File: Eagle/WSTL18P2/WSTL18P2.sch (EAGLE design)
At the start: 22 parts, among them CON1 1X6CONN-1.27-ROUND, CON2 1X6CONN-1.27-ROUND, CON3 1X6CONN-1.27-ROUND, CON4 1X6CONN-1.27-ROUND, T1 ABS07AIG

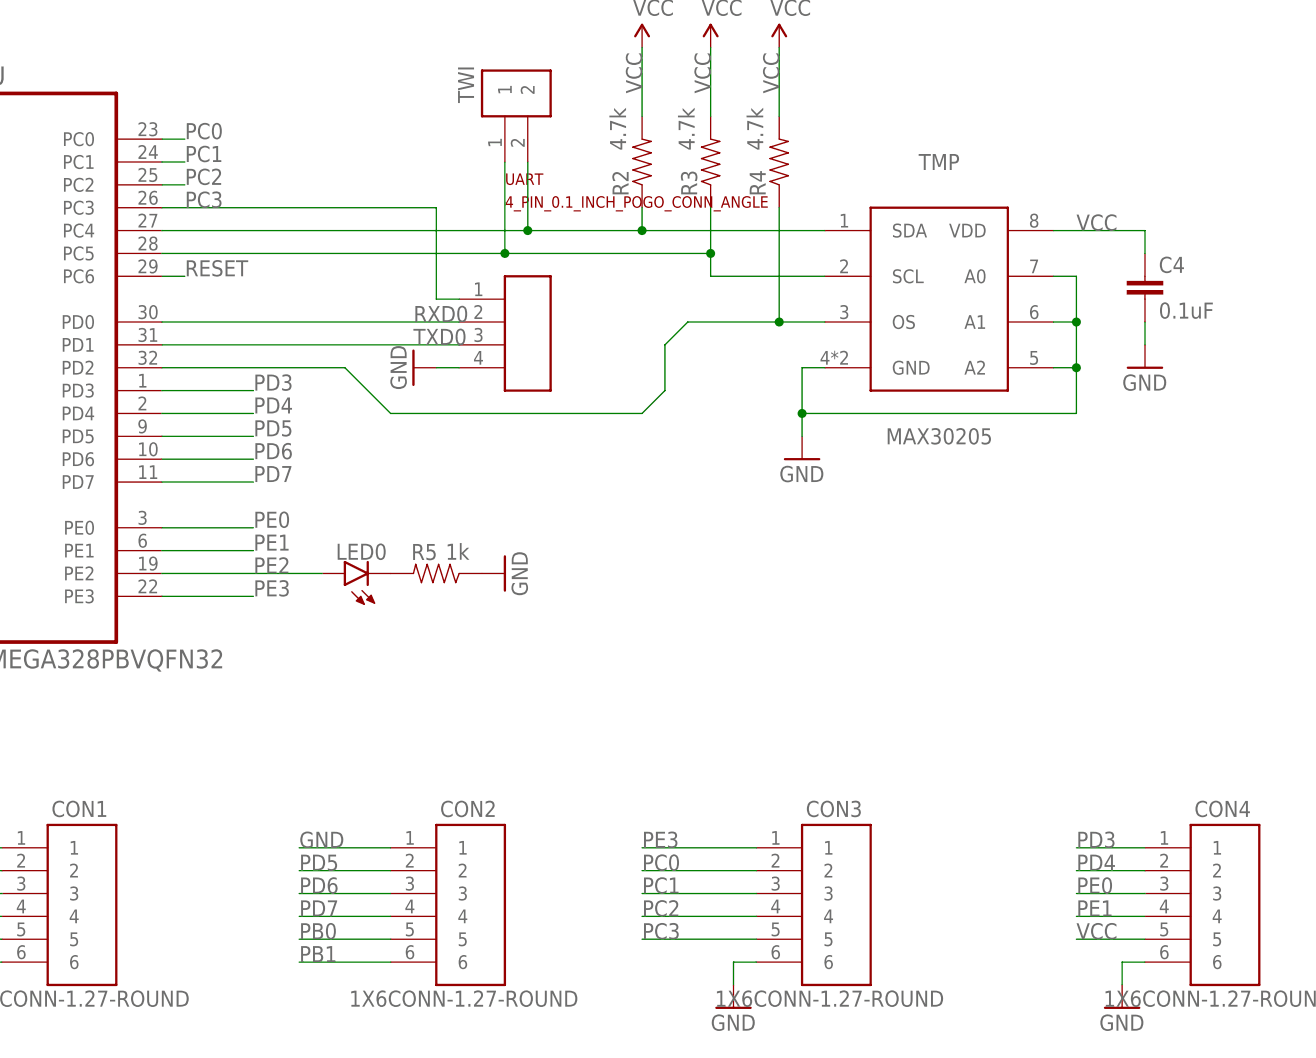
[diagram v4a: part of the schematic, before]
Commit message: Making TWI (I2C) pins available on perimeter headers
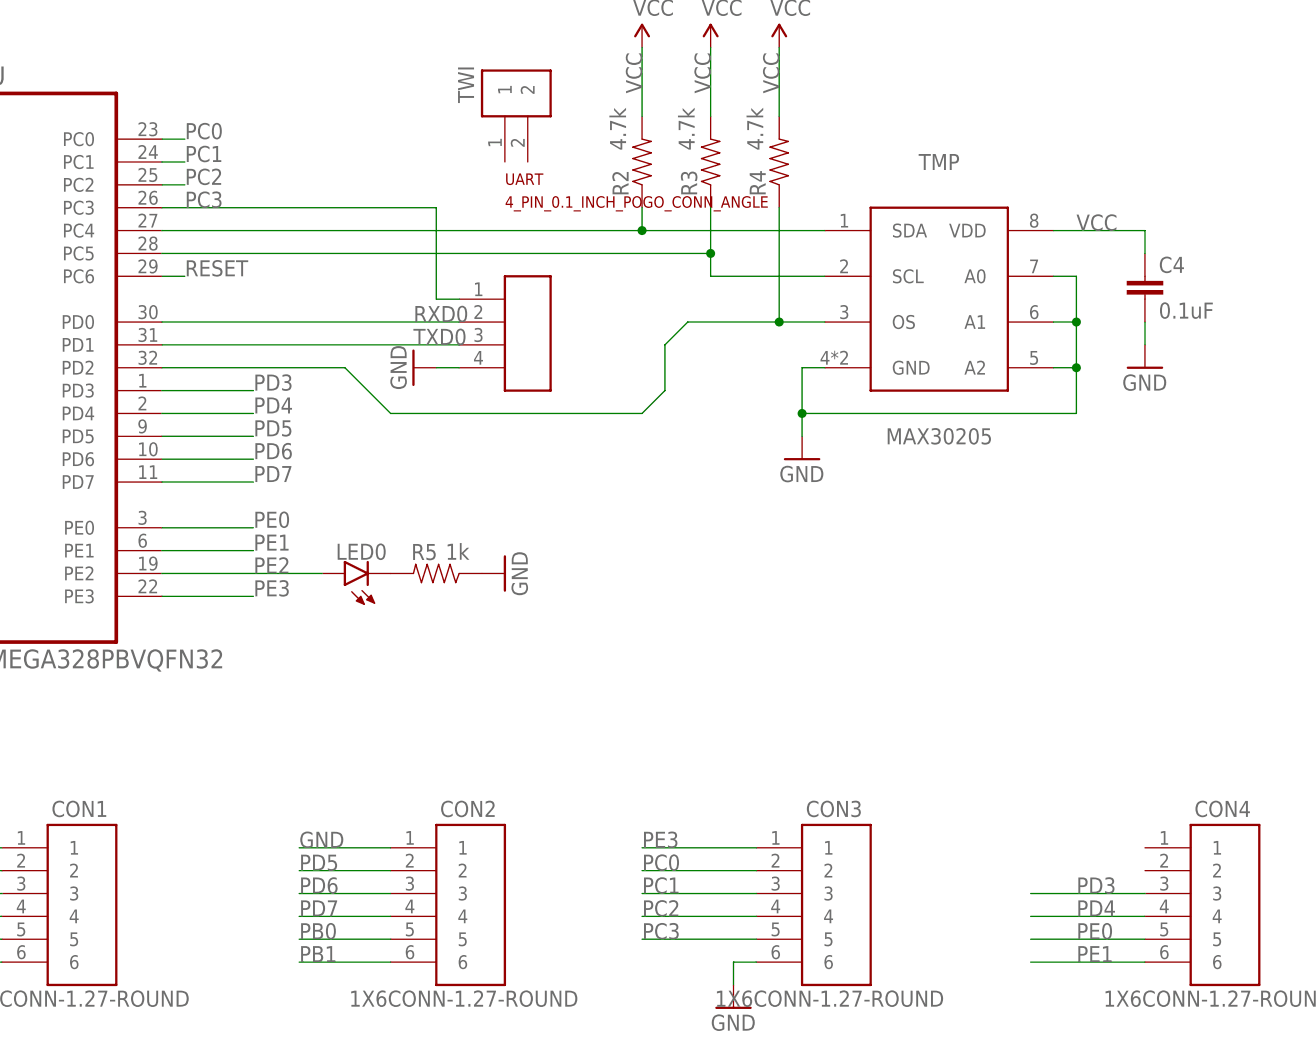
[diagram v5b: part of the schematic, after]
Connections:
- net GND: no longer CON4.6
- net PD3: now also CON4.3; no longer CON4.1
- net PD4: now also CON4.4; no longer CON4.2
- net PE0: now also CON4.5; no longer CON4.3
- net PE1: now also CON4.6; no longer CON4.4
- net SCL0: no longer TWI.1
- net SDA0: no longer TWI.2
- net VCC: no longer CON4.5
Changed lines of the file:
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@@
 <part name="GND9" library="SparkFun-Aesthetics" deviceset="GND" device=""/>
 <part name="CON4" library="AVR_ISP_127" deviceset="1X6CONN-1.27-ROUND" device=""/>
-<part name="GND10" library="SparkFun-Aesthetics" deviceset="GND" device=""/>
 <part name="VCC" library="SparkFun-Aesthetics" deviceset="5V" device="" value="VCC"/>
 <part name="GND11" library="SparkFun-Aesthetics" deviceset="GND" device=""/>
@@
 <instance part="GND9" gate="1" x="149.86" y="-25.4"/>
 <instance part="CON4" gate="G$1" x="205.74" y="-10.16"/>
-<instance part="GND10" gate="1" x="193.04" y="-25.4"/>
 <instance part="VCC" gate="G$1" x="-76.2" y="76.2"/>
 <instance part="GND11" gate="1" x="114.3" y="45.72" rot="R270"/>
@@
 <wire x1="139.7" y1="63.5" x2="139.7" y2="60.96" width="0.1524" layer="91"/>
 <pinref part="MCU" gate="A" pin="PC4"/>
-<wire x1="86.36" y1="60.96" x2="127" y2="60.96" width="0.1524" layer="91"/>
+<wire x1="86.36" y1="60.96" x2="139.7" y2="60.96" width="0.1524" layer="91"/>
 <pinref part="TMP" gate="G$1" pin="SDA"/>
-<wire x1="127" y1="60.96" x2="139.7" y2="60.96" width="0.1524" layer="91"/>
 <wire x1="139.7" y1="60.96" x2="160.02" y2="60.96" width="0.1524" layer="91"/>
 <junction x="139.7" y="60.96"/>
-<pinref part="TWI" gate="G$1" pin="2"/>
-<wire x1="127" y1="68.58" x2="127" y2="60.96" width="0.1524" layer="91"/>
-<junction x="127" y="60.96"/>
 </segment>
 </net>
@@
 <pinref part="R3" gate="G$1" pin="2"/>
 <pinref part="MCU" gate="A" pin="PC5"/>
-<wire x1="86.36" y1="58.42" x2="124.46" y2="58.42" width="0.1524" layer="91"/>
+<wire x1="86.36" y1="58.42" x2="147.32" y2="58.42" width="0.1524" layer="91"/>
 <pinref part="TMP" gate="G$1" pin="SCL"/>
-<wire x1="124.46" y1="58.42" x2="147.32" y2="58.42" width="0.1524" layer="91"/>
 <wire x1="160.02" y1="55.88" x2="147.32" y2="55.88" width="0.1524" layer="91"/>
 <wire x1="147.32" y1="58.42" x2="147.32" y2="55.88" width="0.1524" layer="91"/>
 <wire x1="147.32" y1="63.5" x2="147.32" y2="58.42" width="0.1524" layer="91"/>
 <junction x="147.32" y="58.42"/>
-<pinref part="TWI" gate="G$1" pin="1"/>
-<wire x1="124.46" y1="68.58" x2="124.46" y2="58.42" width="0.1524" layer="91"/>
-<junction x="124.46" y="58.42"/>
 </segment>
 </net>
@@
 <wire x1="68.58" y1="-7.62" x2="60.96" y2="-7.62" width="0.1524" layer="91"/>
 <label x="60.96" y="-7.62" size="1.778" layer="95"/>
-</segment>
-<segment>
-<pinref part="CON4" gate="G$1" pin="5"/>
-<wire x1="195.58" y1="-17.78" x2="187.96" y2="-17.78" width="0.1524" layer="91"/>
-<label x="187.96" y="-17.78" size="1.778" layer="95"/>
 </segment>
 <segment>
@@
 </segment>
 <segment>
-<pinref part="CON4" gate="G$1" pin="6"/>
-<wire x1="195.58" y1="-20.32" x2="193.04" y2="-20.32" width="0.1524" layer="91"/>
-<pinref part="GND10" gate="1" pin="GND"/>
-<wire x1="193.04" y1="-22.86" x2="193.04" y2="-20.32" width="0.1524" layer="91"/>
-</segment>
-<segment>
 <pinref part="GND11" gate="1" pin="GND"/>
 <pinref part="UART" gate="G$1" pin="4"/>
@@
 </segment>
 <segment>
-<pinref part="CON4" gate="G$1" pin="1"/>
-<wire x1="195.58" y1="-7.62" x2="187.96" y2="-7.62" width="0.1524" layer="91"/>
-<label x="187.96" y="-7.62" size="1.778" layer="95"/>
+<label x="187.96" y="-12.7" size="1.778" layer="95"/>
+<wire x1="182.88" y1="-12.7" x2="195.58" y2="-12.7" width="0.1524" layer="91"/>
+<pinref part="CON4" gate="G$1" pin="3"/>
 </segment>
 </net>
@@
 </segment>
 <segment>
-<pinref part="CON4" gate="G$1" pin="2"/>
-<wire x1="195.58" y1="-10.16" x2="187.96" y2="-10.16" width="0.1524" layer="91"/>
-<label x="187.96" y="-10.16" size="1.778" layer="95"/>
+<label x="187.96" y="-15.24" size="1.778" layer="95"/>
+<pinref part="CON4" gate="G$1" pin="4"/>
+<wire x1="182.88" y1="-15.24" x2="195.58" y2="-15.24" width="0.1524" layer="91"/>
 </segment>
 </net>
@@
 </segment>
 <segment>
-<pinref part="CON4" gate="G$1" pin="3"/>
-<wire x1="195.58" y1="-12.7" x2="187.96" y2="-12.7" width="0.1524" layer="91"/>
-<label x="187.96" y="-12.7" size="1.778" layer="95"/>
+<label x="187.96" y="-17.78" size="1.778" layer="95"/>
+<wire x1="182.88" y1="-17.78" x2="195.58" y2="-17.78" width="0.1524" layer="91"/>
+<pinref part="CON4" gate="G$1" pin="5"/>
 </segment>
 </net>
@@
 </segment>
 <segment>
-<pinref part="CON4" gate="G$1" pin="4"/>
-<wire x1="195.58" y1="-15.24" x2="187.96" y2="-15.24" width="0.1524" layer="91"/>
-<label x="187.96" y="-15.24" size="1.778" layer="95"/>
-</segment>
-</net>
+<wire x1="195.58" y1="-20.32" x2="182.88" y2="-20.32" width="0.1524" layer="91"/>
+<label x="187.96" y="-20.32" size="1.778" layer="95"/>
+<pinref part="CON4" gate="G$1" pin="6"/>
+</segment>
+</net>

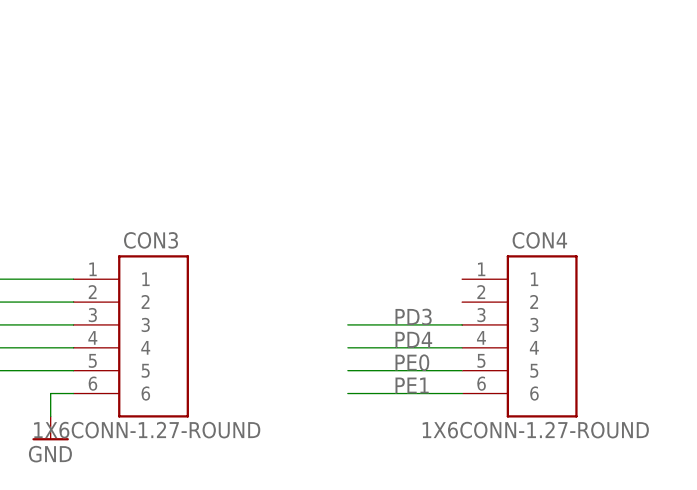
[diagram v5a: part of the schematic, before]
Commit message: Made TWI (I2C) available on perimeter 1.27mm headers
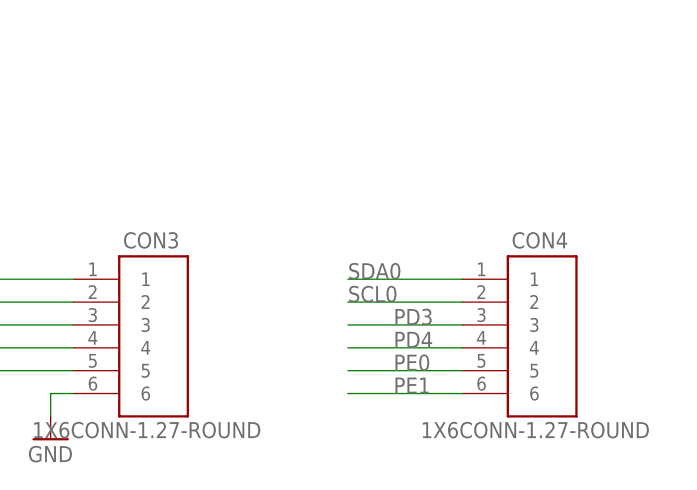
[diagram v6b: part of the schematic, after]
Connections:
- net SCL0: now also CON4.2
- net SDA0: now also CON4.1
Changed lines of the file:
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@@
 <junction x="139.7" y="60.96"/>
+</segment>
+<segment>
+<pinref part="CON4" gate="G$1" pin="1"/>
+<wire x1="195.58" y1="-7.62" x2="182.88" y2="-7.62" width="0.1524" layer="91"/>
+<label x="182.88" y="-7.62" size="1.778" layer="95"/>
 </segment>
 </net>
@@
 <junction x="147.32" y="58.42"/>
 </segment>
+<segment>
+<pinref part="CON4" gate="G$1" pin="2"/>
+<wire x1="195.58" y1="-10.16" x2="182.88" y2="-10.16" width="0.1524" layer="91"/>
+<label x="182.88" y="-10.16" size="1.778" layer="95"/>
+</segment>
 </net>

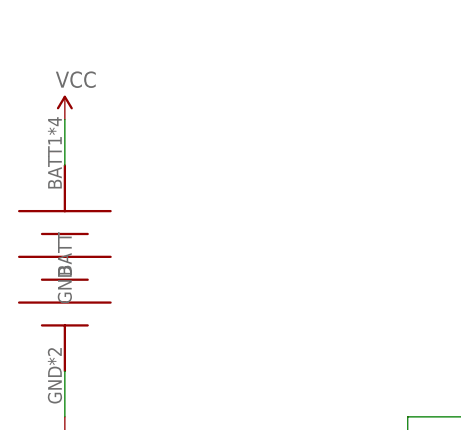
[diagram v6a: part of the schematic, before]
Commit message: Added pads on the positive battery holder contacts
This will allow use of both SMD and through-hole versions of the battery holder
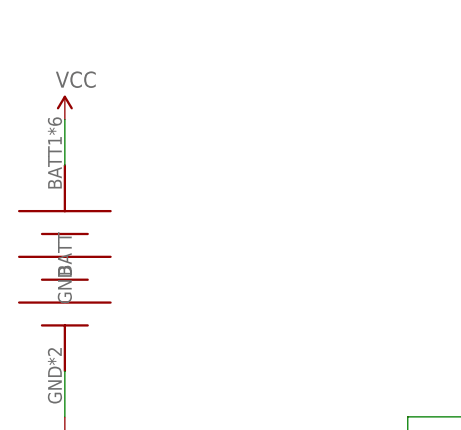
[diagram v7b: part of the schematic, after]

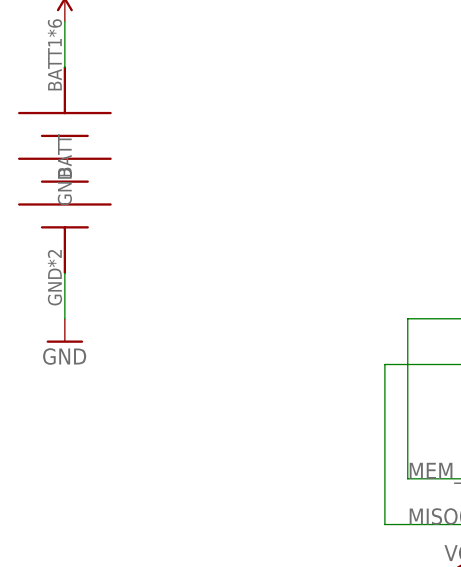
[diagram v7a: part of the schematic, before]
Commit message: Moved battery GND pad to a sincle circular in centre
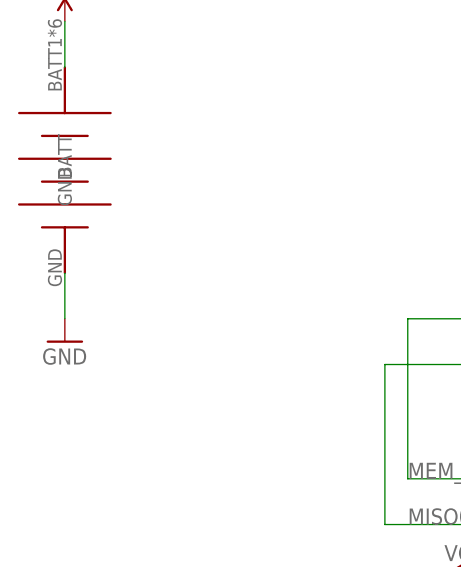
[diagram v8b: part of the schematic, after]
